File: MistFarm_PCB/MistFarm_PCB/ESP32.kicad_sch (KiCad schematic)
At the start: 43 parts, among them J5 GRPB052VWVN-RC, J6 OLED, Q3 UMH3N, U2 ESP32-WROOM-32E, U6 CP2104, U9 USBLC6-2P6

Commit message: add sch
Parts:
- J6: value OLED -> I2C
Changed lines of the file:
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@@
 		(on_board yes)
 		(dnp no)
-		(fields_autoplaced yes)
 		(property "Reference" "#PWR050"
 			(at 223.52 62.23 0)
@@
 		)
 		(property "Value" "GND"
-			(at 223.52 63.5 0)
+			(at 227.076 67.056 0)
 			(effects
 				(font
@@
 			)
 		)
-		(property "Value" "OLED"
+		(property "Value" "I2C"
 			(at 199.39 160.0199 0)
 			(effects

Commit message: sch and pcb modify
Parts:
- renumbered C38 to C1, C24 to C10, C25 to C11, C26 to C12, C33 to C13, C34 to C14, C12 to C15, C39 to C16, C40 to C17, C41 to C18, C32 to C2, C11 to C3, C20 to C4, C21 to C5, C22 to C6, C36 to C7, C7 to C8, C23 to C9, F2 to F1, FL2 to FL1, J5 to J1, J6 to J2, Q3 to Q1, R16 to R1, R24 to R10, R25 to R11, R26 to R12, R27 to R13, R28 to R14, R29 to R15, R17 to R2, R18 to R3, R19 to R4, R31 to R5, R20 to R6, R23 to R7, R34 to R8, R35 to R9, S2 to S1, U2 to U1, U6 to U2, U9 to U3, UART2 to UART1
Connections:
- net 5A OUT: now reaches FL1.2, UART1.A4 (VBUS), UART1.A9 (VBUS), UART1.B4 (VBUS), UART1.B9 (VBUS)
- net Temp_Sensor: now reaches U1.10 (IO25)
- no-connect marks 16 -> 22

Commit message: PCB update
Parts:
- added J4: 61300511121, 61300511121:61300511121, symbol 6130XX11121_61300511121:6130XX11121_61300511121
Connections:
- net 3.3V OUT: now also J4.1
- net 5A OUT: now also UART1.A4_B9 (VBUS), UART1.B4_A9 (VBUS); no longer UART1.A4 (VBUS)
- net GND: now also UART1.A1_B12 (GND), UART1.B1_A12 (GND), UART1.SH1 (SHIELD), UART1.SH2 (SHIELD), UART1.SH3 (SHIELD), UART1.SH4 (SHIELD), J4.2; no longer UART1.A1 (GND), UART1.S1 (SHIELD)
- net I2C_SCL: now also J4.4
- net I2C_SDL: now also J4.5
- net Temp_Sensor: now also J4.3

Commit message: PCB update
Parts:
- J2: value I2C -> HTSW-104-20-TM-S
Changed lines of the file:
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@@
 			)
 		)
-		(property "Value" "I2C"
+		(property "Value" "HTSW-104-20-TM-S"
 			(at 199.39 160.0199 0)
 			(effects

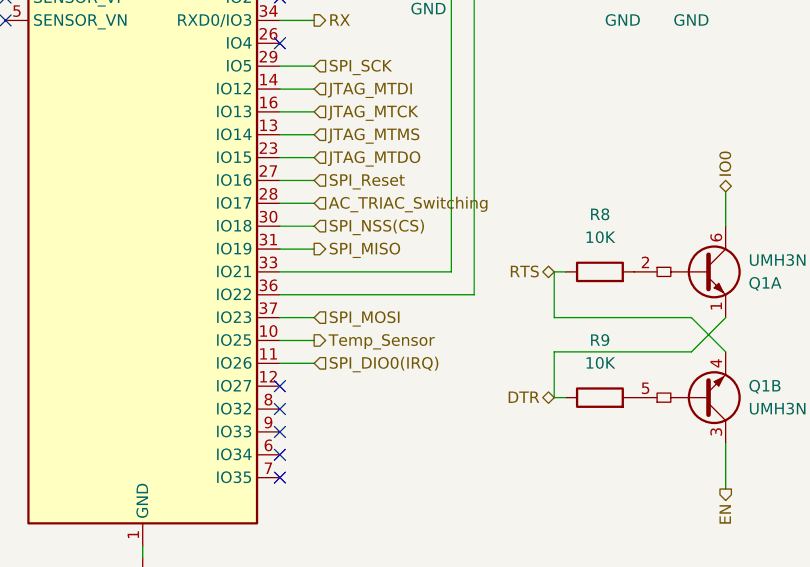
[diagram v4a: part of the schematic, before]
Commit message: code mold adding and sch gps add
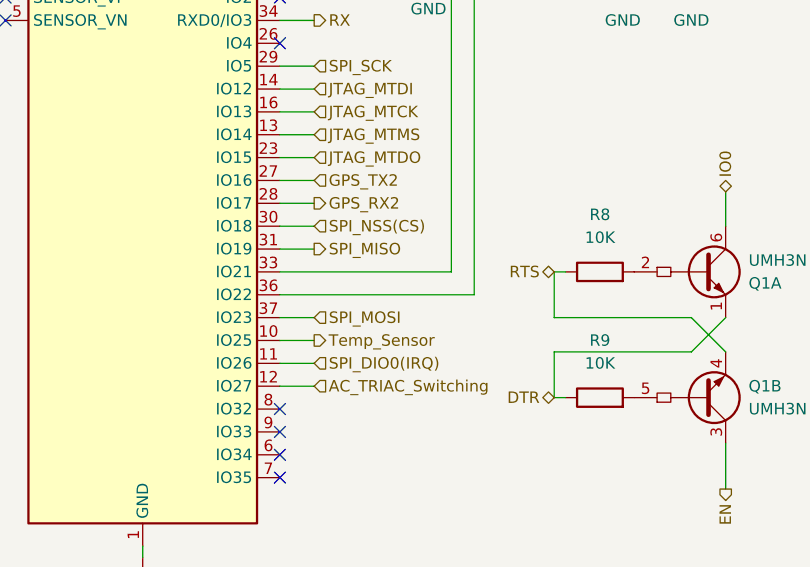
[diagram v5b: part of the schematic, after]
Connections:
- net AC_TRIAC_Switching: now also U1.12 (IO27); no longer U1.28 (IO17)
- net SPI_Reset renamed GPS_TX2
- new net GPS_RX2: U1.28 (IO17)
- no-connect marks 22 -> 21
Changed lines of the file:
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@@
-	)
-	(no_connect
-		(at 97.79 115.57)
 	)
 	(no_connect
@@
 		(pts
 			(xy 77.47 162.56) (xy 87.63 162.56)
+		)
+		(stroke
+			(width 0)
+			(type default)
+		)
+	)
+	(wire
+		(pts
+			(xy 97.79 115.57) (xy 101.6 115.57)
 		)
 		(stroke
@@
 		)
 	)
+	(hierarchical_label "GPS_RX2"
+		(shape output)
+		(at 101.6 95.25 0)
+		(effects
+			(font
+				(size 1.27 1.27)
+			)
+			(justify left)
+		)
+	)
 	(hierarchical_label "JTAG_MTDO"
 		(shape output)
@@
 		)
 	)
-	(hierarchical_label "SPI_Reset"
-		(shape input)
-		(at 101.6 92.71 0)
-		(effects
-			(font
-				(size 1.27 1.27)
-			)
-			(justify left)
-		)
-	)
 	(hierarchical_label "SPI_MISO"
 		(shape output)
@@
 		)
 	)
-	(hierarchical_label "AC_TRIAC_Switching"
-		(shape input)
-		(at 101.6 95.25 0)
-		(effects
-			(font
-				(size 1.27 1.27)
-			)
-			(justify left)
-		)
-	)
 	(hierarchical_label "SPI_MOSI"
 		(shape input)
@@
 		)
 	)
+	(hierarchical_label "GPS_TX2"
+		(shape input)
+		(at 101.6 92.71 0)
+		(effects
+			(font
+				(size 1.27 1.27)
+			)
+			(justify left)
+		)
+	)
 	(hierarchical_label "JTAG_MTDI"
 		(shape output)
@@
 		(effects
 			(font
+				(size 1.27 1.27)
+			)
+			(justify left)
+		)
+	)
+	(hierarchical_label "AC_TRIAC_Switching"
+		(shape input)
+		(at 101.6 115.57 0)
+		(effects
+			(font

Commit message: PCB end
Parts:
- removed C14, C16: 22uF, Capacitor_SMD:C_0805_2012Metric, symbol Device:C
- removed C15, C18: 4.7uF, Capacitor_SMD:C_0603_1608Metric, symbol Device:C
- removed C17: 0.1uF, Capacitor_SMD:C_0603_1608Metric, symbol Device:C
- removed F1: 0603L100SLYR, Resistor_SMD:R_0603_1608Metric, symbol Device:Polyfuse
- removed FL1: BLM21PG221SN1D, BLM21PG221SN1D:BEADC2012X105N, symbol BLM21PG221SN1D:BLM21PG221SN1D
- removed R13: 10K, Resistor_SMD:R_0603_1608Metric, symbol Device:R
- removed R14, R15: 5.1K, Resistor_SMD:R_0402_1005Metric, symbol Device:R
- removed UART1: 12402012E212A, 12402012E212A:AMPHENOL_12402012E212A, symbol Connector:USB_C_Receptacle_USB2.0_16P
- added J4: 12402012E212A, 12402012E212A:AMPHENOL_12402012E212A, symbol Connector:USB_C_Receptacle_USB2.0_16P
- C13: value 0.1uF -> 10uF; footprint Capacitor_SMD:C_0603_1608Metric -> Capacitor_SMD:C_0805_2012Metric
- R11, R12: value 22R -> 5.1K
- renumbered J4 to J1, J1 to J2, J2 to J3
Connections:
- net 3.3V OUT: now also U2.7 (REGIN)
- net 5A OUT: now also U2.8 (VBUS), U3.5 (VBUS), J4.A4_B9 (VBUS), J4.A9 (VBUS), J4.B4 (VBUS), J4.B4_A9 (VBUS), J4.B9 (VBUS)
- net GND: now also R11.1, R12.1, J4.A12 (GND), J4.A1_B12 (GND), J4.B1 (GND), J4.B12 (GND), J4.B1_A12 (GND), J4.SH1 (SHIELD), J4.SH2 (SHIELD), J4.SH3 (SHIELD), J4.SH4 (SHIELD)
- net RX: now also U2.21 (TXD); no longer R12.1
- net TX: now also U2.20 (RXD); no longer R11.1
- net at R11.2: now also J4.B5 (CC2); no longer U2.20 (RXD)
- net at R12.2: now also J4.A5 (CC1); no longer U2.21 (TXD)
- net at U2.3 (D+): now also U3.4 (I/O2); no longer U3.6 (I/O1)
- net at U2.4 (D-): now also U3.6 (I/O1); no longer U3.4 (I/O2)
- net at U3.1 (I/O1): now also J4.A7 (D-), J4.B7 (D-)
- net at U3.3 (I/O2): now also J4.A6 (D+), J4.B6 (D+)
- net GPS_RX2: no longer names the net of U1.28 (IO17)
- no-connect marks 21 -> 23
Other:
- moved on the sheet: C11, C12, J3

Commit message: PCB real end
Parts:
- removed C3, C4, C5, C6: PESD0402-140, PESD0402-140:RESC1005X35N, symbol PESD0402-140:PESD0402-140
- removed J2: GRPB052VWVN-RC, Varistor:SULLINS_GRPB052VWVN-RC, symbol GRPB052VWVN-RC:GRPB052VWVN-RC
- removed J3: HTSW-104-20-TM-S, HTSW-104-20-TM-S:SAMTEC_HTSW-104-20-TM-S, symbol HTSW-104-20-TM-S:HTSW-104-20-TM-S
- removed R1, R2, R3, R4: 100R, Resistor_SMD:R_0603_1608Metric, symbol Device:R
- added C17, C19: 4.7uF, Capacitor_SMD:C_0603_1608Metric, symbol Device:C
- added C18, C20: 0.1uF, Capacitor_SMD:C_0603_1608Metric, symbol Device:C
- added C21: 1uF, Capacitor_SMD:C_0603_1608Metric, symbol Device:C
- added C22: 22uF, Capacitor_SMD:C_0805_2012Metric, symbol Device:C
- added J2, J3, J6: 6130XX11121_61300811121, 61300811121:61300811121, symbol 6130XX11121_61300811121:6130XX11121_61300811121
- added U6: L86-M33, L86-M33:XCVR_L86-M33, symbol L86-M33:L86-M33
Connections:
- net 3.3V OUT: now also C11.2, C12.2, C17.2, C18.2, C19.2, C20.2, C21.1, C22.1, J2.1, J3.1, J6.1, U6.4 (VCC), U6.5 (V_BCKP); no longer C11.1, C12.1
- net GND: now also C11.1, C12.1, C17.1, C18.1, C19.1, C20.1, C21.2, C22.2, J2.2, J3.2, J3.3, J6.2, U6.12 (GND), U6.3 (GND); no longer C11.2, C12.2
- net GPIO2: now reaches U1.24 (IO2)
- net GPIO2: now also J2.8
- net GPIO4: now reaches U1.26 (IO4)
- net GPIO4: now also J2.7
- net GPIO17: now reaches U1.28 (IO17)
- net GPIO17: now also J3.6
- net GPIO34: now reaches U1.6 (IO34)
- net GPIO34: now also J6.4
- net GPIO35: now reaches U1.7 (IO35)
- net GPIO35: now also J6.3
- net GPIO32: now reaches U1.8 (IO32)
- net GPIO32: now also J6.6
- net GPIO33: now reaches U1.9 (IO33)
- net GPIO33: now also J6.5
- net GPS_TX2 renamed GPIO16
- net GPIO16: now also J3.7
- net JTAG_MTCK renamed GPIO13
- net GPIO13: now also J2.4, U6.1 (RXD1)
- net JTAG_MTDI renamed GPIO12
- net GPIO12: now also J2.5, U6.10 (~{RESET})
- net JTAG_MTDO renamed GPIO15
- net GPIO15: now also J3.8
- net JTAG_MTMS renamed GPIO14
- net GPIO14: now also J2.3, U6.2 (TXD1)
- net SPI_DIO0(IRQ) renamed GPIO26
- net GPIO26: now also J6.7
- net SPI_MISO renamed GPIO19
- net SPI_MOSI renamed GPIO23
- net GPIO23: now also J6.8
- net SPI_NSS(CS) renamed GPIO18
- net SPI_SCK renamed GPIO5
- net GPIO5: now also J2.6
- new net Moter_A: J3.5
- new net Moter_B: J3.4
- no-connect marks 23 -> 20
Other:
- moved on the sheet: C11, C12
